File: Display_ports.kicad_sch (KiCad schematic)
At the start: 52 parts, among them J2 DP_A, J3 DP_B, J4 DP_C, J5 eDP 4-lane 40-pin ipex, Q1 2N7002, Q2 2N7002, Q3 2N7002, Q4 2N7002, Q5 2N7002, Q6 2N7002

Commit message: Added LGA1151 socket bracket holes
stolen from another lga1151 footprint that has wrong pin numbers....
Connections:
- net GND: now also J2.19 (DP_PWR_RETURN), J3.19 (DP_PWR_RETURN), J4.19 (DP_PWR_RETURN)
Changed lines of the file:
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@@
+	)
+	(junction
+		(at 356.87 227.33)
+		(diameter 0)
+		(color 0 0 0 0)
 	)
 	(junction
@@
 	)
 	(junction
+		(at 356.87 77.47)
+		(diameter 0)
+		(color 0 0 0 0)
+	)
+	(junction
 		(at 86.36 172.72)
 		(diameter 0)
@@
 	)
 	(junction
+		(at 356.87 153.67)
+		(diameter 0)
+		(color 0 0 0 0)
+	)
+	(junction
 		(at 97.79 275.59)
 		(diameter 0)
@@
 	(wire
 		(pts
+			(xy 356.87 153.67) (xy 358.14 153.67)
+		)
+		(stroke
+			(width 0)
+			(type default)
+		)
+	)
+	(wire
+		(pts
 			(xy 231.14 36.83) (xy 232.41 36.83)
 		)
@@
 	(wire
 		(pts
+			(xy 356.87 77.47) (xy 358.14 77.47)
+		)
+		(stroke
+			(width 0)
+			(type default)
+		)
+	)
+	(wire
+		(pts
 			(xy 389.89 115.57) (xy 389.89 162.56)
 		)
@@
 	(wire
 		(pts
-			(xy 356.87 133.35) (xy 356.87 162.56)
+			(xy 356.87 227.33) (xy 358.14 227.33)
+		)
+		(stroke
+			(width 0)
+			(type default)
+		)
+	)
+	(wire
+		(pts
+			(xy 356.87 133.35) (xy 356.87 153.67)
 		)
 		(stroke
@@
 	(wire
 		(pts
+			(xy 356.87 227.33) (xy 356.87 236.22)
+		)
+		(stroke
+			(width 0)
+			(type default)
+		)
+	)
+	(wire
+		(pts
 			(xy 252.73 52.07) (xy 255.27 52.07)
 		)
@@
 	(wire
 		(pts
+			(xy 356.87 153.67) (xy 356.87 162.56)
+		)
+		(stroke
+			(width 0)
+			(type default)
+		)
+	)
+	(wire
+		(pts
 			(xy 330.2 58.42) (xy 355.6 58.42)
 		)
@@
 	(wire
 		(pts
-			(xy 356.87 207.01) (xy 356.87 236.22)
+			(xy 356.87 207.01) (xy 356.87 227.33)
 		)
 		(stroke
@@
 	(wire
 		(pts
+			(xy 356.87 77.47) (xy 356.87 86.36)
+		)
+		(stroke
+			(width 0)
+			(type default)
+		)
+	)
+	(wire
+		(pts
 			(xy 355.6 181.61) (xy 355.6 182.88)
 		)
@@
 	(wire
 		(pts
-			(xy 356.87 57.15) (xy 356.87 86.36)
-		)
-		(stroke
+			(xy 356.87 57.15) (xy 356.87 77.47)
+		)
+		(stroke

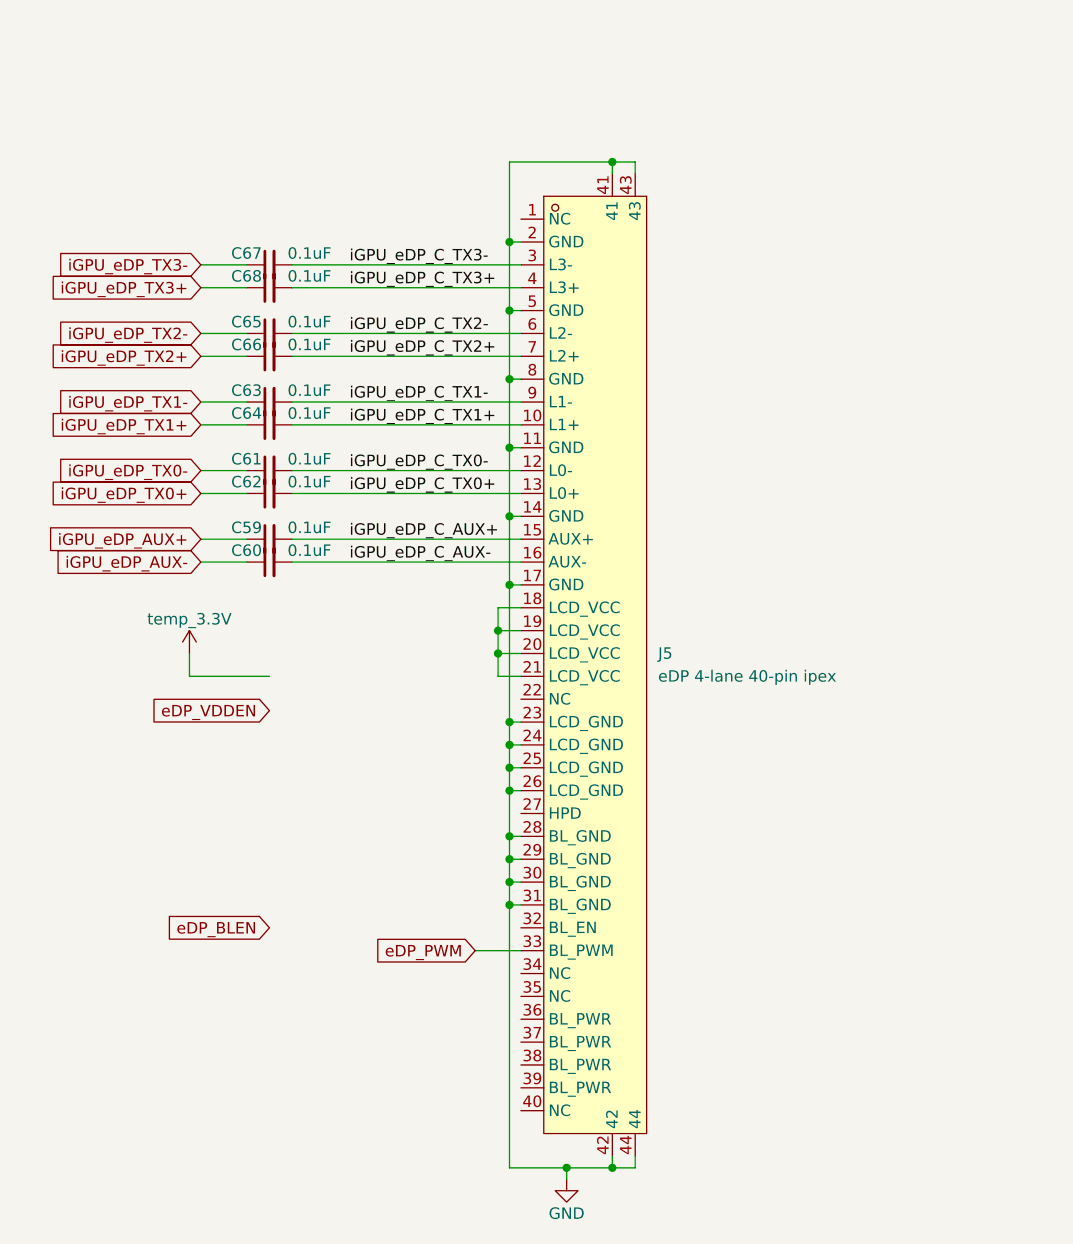
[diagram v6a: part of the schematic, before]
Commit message: Added CPU CFG resistors
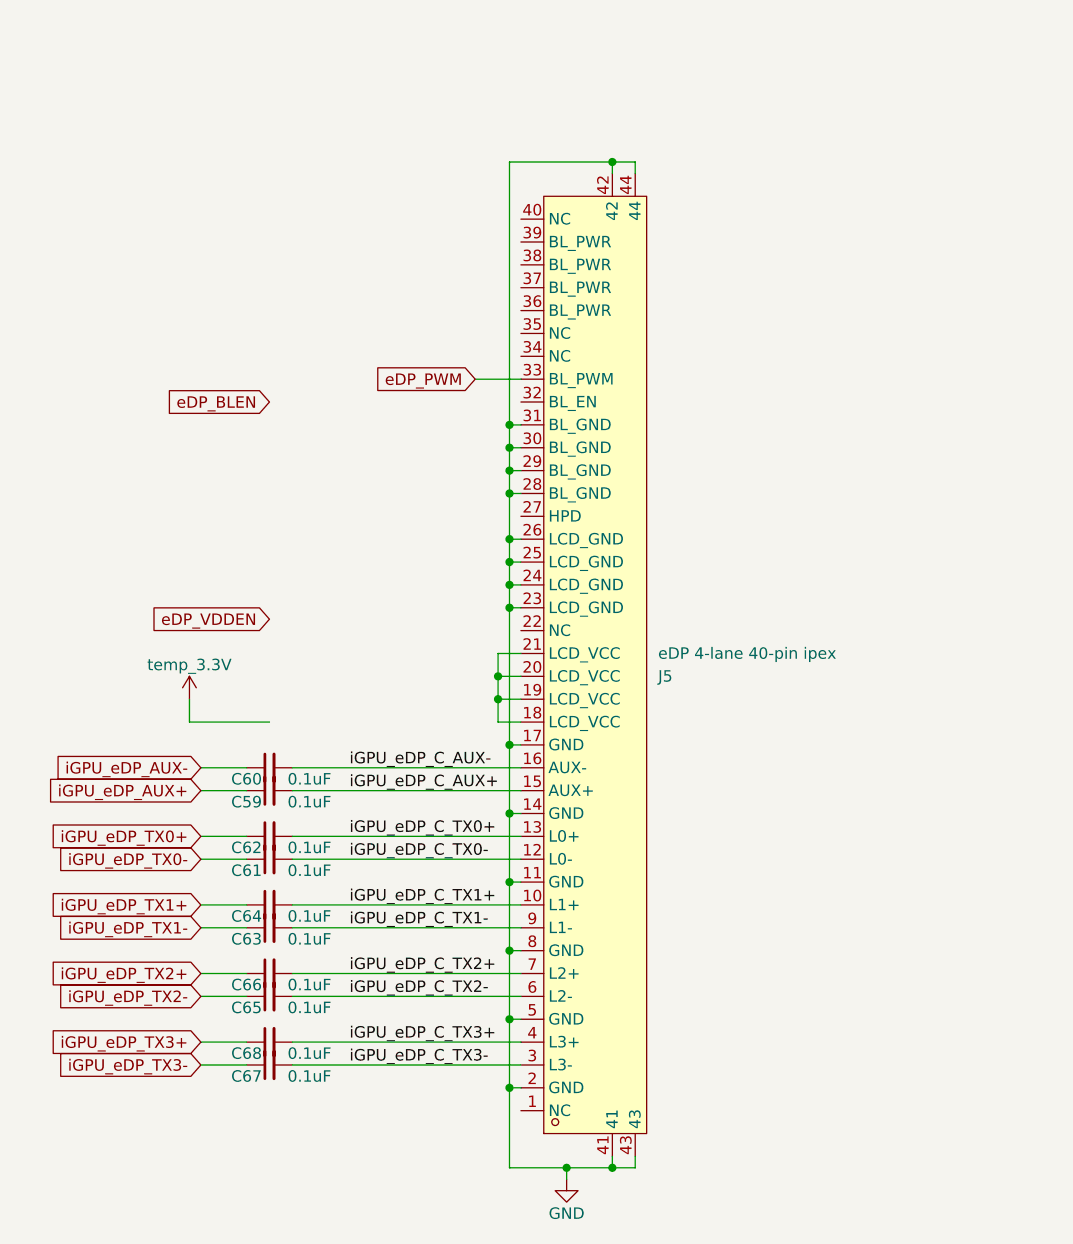
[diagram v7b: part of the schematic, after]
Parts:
- J5: footprint (none) -> A-my-stuff:40pIPEX_20455-040E-76
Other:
- moved on the sheet: C59, C60, C61, C62, C63, C64, C65, C66, C67, C68
